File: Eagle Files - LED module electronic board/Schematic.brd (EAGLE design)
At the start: 30.5 x 30.5 mm, 14 parts, among them IC1 AMS1117-1.5, IC2 LM358N, J1 2.54 CONN, J2 2.54 CONN, Q1 P16NF06L

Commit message: Update
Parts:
- removed J1, J2: 2.54 CONN, SparkFun-Connectors:1X02
- removed Q1: P16NF06L, adafruit:TO220V
- removed R3: 10k, LED-microscope-library:HDRV3W64P254_1X3_1016X508X838B
- added Q2: P16NF06L, transistor-power:TO220BV
- added U$1: (no value), untitled:POT-SWITCH-PTH
- added U$3, U$4: (no value), untitled:1X02_NO_SILK
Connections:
- new net N$10: IC2.5, U$1.2
- net GND: now also U$1.3, U$3.2; no longer J1.1, R3.1
- net N$1: now also U$1.5, U$3.1; no longer IC2.5, R3.3
- net N$4: now also U$1.1; no longer R3.2
- net N$5: now also Q2.D, U$4.1; no longer J2.2, Q1.2
- net N$7: now also Q2.G; no longer Q1.1
- net N$9: now also Q2.S; no longer Q1.3
- net VCC: now also U$1.4, U$4.2; no longer J1.2, J2.1
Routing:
- net N$10: track 0.00 -> 20.1 mm, vias 0 -> 1
- net N$5: track 20.6 -> 26.9 mm
- net N$4: track 11.3 -> 17.1 mm
- net N$1: track 16.2 -> 17.1 mm
- net N$9: track 19.0 -> 19.6 mm

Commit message: Major changes!
Major changes! Do not use older version, pins swapped in V-regulator.
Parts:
- removed IC1: AMS1117-1.5, linear:SOT223
- added U$2: VREG-AMS1117-1.5, untitled:SOT230P700X180-4
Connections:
- net GND: now also U$2.1; no longer IC1.4
- net N$3: now also U$2.2, U$2.4; no longer IC1.3
- net VCC: now also U$2.3; no longer IC1.1
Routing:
- net N$3: track 15.9 -> 18.6 mm
- net VCC: track 40.9 -> 39.7 mm
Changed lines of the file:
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@@
 </layers>
 <board>
-<fusionsync huburn="a.cGVyc29uYWw6dWUyYjI2N2I0" projecturn="a.cGVyc29uYWw6dWUyYjI2N2I0IzIwMTcwOTAxOTA2NzgyODE" f3durn="urn:adsk.wipprod:dm.lineage:6GncY3L6S8qHhpXXGHIO-A" pcbguid="c076c7f6-f98b-4770-9c04-7120ef74dbe8" lastpulledtime="" lastsyncedchangeguid="168a07d3-ac94-f938-486a-87856d6dfaa1"/>
+<fusionsync huburn="a.cGVyc29uYWw6dWUyYjI2N2I0" projecturn="a.cGVyc29uYWw6dWUyYjI2N2I0IzIwMTcwOTAxOTA2NzgyODE" f3durn="urn:adsk.wipprod:dm.lineage:6GncY3L6S8qHhpXXGHIO-A" pcbguid="c076c7f6-f98b-4770-9c04-7120ef74dbe8" lastpulledtime="" lastsyncedchangeguid="b84cecf9-df35-d3de-ebe7-257acc63ca98"/>
 <plain>
 <wire x1="1.5875" y1="68.2625" x2="32.0475" y2="68.2625" width="0" layer="20"/>
@@
 <attribute name="VALUE" x="25.781" y="88.9635" size="1.27" layer="27" ratio="10" rot="R270"/>
 </element>
-<element name="IC1" library="linear" library_urn="urn:adsk.eagle:library:262" package="SOT223" package3d_urn="urn:adsk.eagle:package:28541/2" value="AMS1117-1.5" x="8.255" y="83.82" smashed="yes" rot="MR0">
-<attribute name="NAME" x="4.445" y="81.9658" size="1.27" layer="26" rot="MR0"/>
-<attribute name="VALUE" x="10.795" y="82.4992" size="1.27" layer="28" rot="MR0"/>
-</element>
 <element name="IC2" library="linear" library_urn="urn:adsk.eagle:library:262" package="DIL08" package3d_urn="urn:adsk.eagle:package:16409/2" value="LM358N" x="20.955" y="83.82" smashed="yes" rot="R270">
 <attribute name="NAME" x="18.034" y="89.154" size="1.27" layer="25" ratio="10"/>
@@
 <attribute name="VALUE" x="23.495" y="83.185" size="1.27" layer="27" ratio="10" rot="R270"/>
 </element>
+<element name="U$2" library="untitled" library_urn="urn:adsk.eagle:library:8804918" package="SOT230P700X180-4" package3d_urn="urn:adsk.eagle:package:9947855/1" value="VREG-AMS1117-1.5" x="8.255" y="83.5025" smashed="yes" rot="MR270">
+<attribute name="NAME" x="4.1214" y="83.5025" size="1.27" layer="26" rot="MR270" align="bottom-center"/>
+<attribute name="VALUE" x="12.24" y="83.5025" size="1.27" layer="28" rot="MR270" align="top-center"/>
+</element>
 </elements>
 <signals>
 <signal name="GND">
-<contactref element="IC1" pad="4"/>
 <contactref element="IC2" pad="4"/>
 <contactref element="R2" pad="1"/>
@@
 <contactref element="U$3" pad="2"/>
 <contactref element="U$1" pad="3"/>
-<wire x1="8.255" y1="86.919" x2="8.255" y2="94.615" width="0" layer="19" extent="16-16"/>
-<wire x1="4.705" y1="86.36" x2="8.255" y2="86.919" width="0" layer="19" extent="1-16"/>
-<wire x1="14.605" y1="88.417" x2="8.255" y2="86.919" width="0" layer="19" extent="16-16"/>
-<wire x1="6.655" y1="78.74" x2="4.705" y2="86.36" width="0" layer="19" extent="1-1"/>
+<contactref element="U$2" pad="1"/>
+<wire x1="8.255" y1="94.615" x2="15.955" y2="97.155" width="0" layer="19" extent="1-1"/>
+<wire x1="14.605" y1="88.417" x2="15.955" y2="97.155" width="0" layer="19" extent="16-16"/>
 <wire x1="17.145" y1="80.01" x2="14.605" y2="88.417" width="0" layer="19" extent="16-16"/>
 <wire x1="23.755" y1="75.565" x2="17.145" y2="80.01" width="0" layer="19" extent="1-1"/>
-<wire x1="15.955" y1="97.155" x2="6.655" y2="78.74" width="0" layer="19" extent="1-1"/>
+<wire x1="4.705" y1="86.36" x2="8.255" y2="94.615" width="0" layer="19" extent="1-1"/>
+<wire x1="6.655" y1="78.74" x2="4.705" y2="86.36" width="0" layer="19" extent="1-1"/>
+<wire x1="5.955" y1="86.5251" x2="6.655" y2="78.74" width="0" layer="19" extent="1-1"/>
 </signal>
 <signal name="N$3">
-<contactref element="IC1" pad="3"/>
 <contactref element="R1" pad="1"/>
 <contactref element="C2" pad="+"/>
-<wire x1="5.7023" y1="80.8101" x2="5.9436" y2="80.7212" width="0.3556" layer="16"/>
-<wire x1="9.855" y1="78.74" x2="9.855" y2="77.775" width="0.3556" layer="1"/>
-<wire x1="5.9436" y1="80.7212" x2="6.0325" y2="80.6323" width="0.3556" layer="16"/>
+<wire x1="9.855" y1="77.775" x2="9.855" y2="78.74" width="0.3556" layer="1"/>
 <wire x1="14.453" y1="79.223" x2="14.605" y2="79.223" width="0.3556" layer="16"/>
 <wire x1="14.605" y1="79.223" x2="12.5345" y2="77.1525" width="0.3556" layer="16"/>
-<wire x1="12.5345" y1="77.1525" x2="8.255" y2="77.1525" width="0.3556" layer="16"/>
-<wire x1="9.855" y1="77.775" x2="9.2325" y2="77.1525" width="0.3556" layer="1"/>
-<wire x1="9.2325" y1="77.1525" x2="8.255" y2="77.1525" width="0.3556" layer="1"/>
-<via x="8.255" y="77.1525" extent="1-16" drill="0.3556"/>
-<wire x1="8.255" y1="77.1525" x2="6.6675" y2="77.1525" width="0.3556" layer="16"/>
-<wire x1="6.6675" y1="77.1525" x2="6.0325" y2="77.7875" width="0.3556" layer="16"/>
-<wire x1="6.0325" y1="77.7875" x2="6.0325" y2="80.6323" width="0.3556" layer="16"/>
+<via x="10.7127" y="77.1525" extent="1-16" drill="0.3556"/>
+<wire x1="10.7127" y1="77.1525" x2="10.16" y2="77.1525" width="0.356" layer="1"/>
+<wire x1="10.16" y1="77.1525" x2="9.855" y2="77.4575" width="0.356" layer="1"/>
+<wire x1="9.855" y1="77.4575" x2="9.855" y2="77.775" width="0.356" layer="1"/>
+<wire x1="12.5345" y1="77.1525" x2="10.7127" y2="77.1525" width="0.356" layer="16"/>
+<wire x1="8.89" y1="77.1525" x2="8.255" y2="77.7875" width="0.356" layer="16"/>
+<wire x1="8.89" y1="77.1525" x2="10.7127" y2="77.1525" width="0.356" layer="16"/>
+<contactref element="U$2" pad="2"/>
+<contactref element="U$2" pad="4"/>
+<wire x1="8.255" y1="77.7875" x2="8.255" y2="80.4799" width="0.356" layer="16"/>
+<wire x1="8.255" y1="80.4799" x2="8.255" y2="86.5251" width="1.067" layer="16"/>
 </signal>
 <signal name="VCC">
-<contactref element="IC1" pad="1"/>
 <contactref element="C1" pad="+"/>
 <contactref element="IC2" pad="8"/>
-<wire x1="10.45754375" y1="80.645" x2="10.5664" y2="80.7212" width="0.3556" layer="16"/>
-<wire x1="10.16" y1="81.1276" x2="10.5664" y2="80.7212" width="0.3556" layer="16"/>
 <wire x1="24.765" y1="87.63" x2="23.495" y2="86.36" width="0.3556" layer="1"/>
 <wire x1="23.495" y1="86.36" x2="11.805" y2="86.36" width="0.3556" layer="1"/>
-<wire x1="10.5664" y1="80.7212" x2="10.6426" y2="80.645" width="1.067" layer="16"/>
 <wire x1="11.805" y1="86.36" x2="11.805" y2="83.82" width="1.067" layer="1"/>
-<wire x1="10.5664" y1="80.7212" x2="10.5664" y2="82.5814" width="1.067" layer="16"/>
-<wire x1="10.5664" y1="82.5814" x2="11.805" y2="83.82" width="1.067" layer="16"/>
 <via x="11.805" y="83.82" extent="1-16" drill="1.067"/>
 <wire x1="11.7475" y1="86.4175" x2="11.805" y2="86.36" width="1.067" layer="1"/>
@@
 <wire x1="11.805" y1="73.4" x2="10.795" y2="72.39" width="1.067" layer="1"/>
 <wire x1="11.805" y1="83.82" x2="11.805" y2="73.4" width="1.067" layer="1"/>
+<contactref element="U$2" pad="3"/>
+<wire x1="10.555" y1="85.07" x2="10.555" y2="86.5251" width="1.067" layer="16"/>
+<wire x1="11.805" y1="83.82" x2="10.555" y2="85.07" width="1.067" layer="16"/>
 </signal>
 <signal name="N$2">

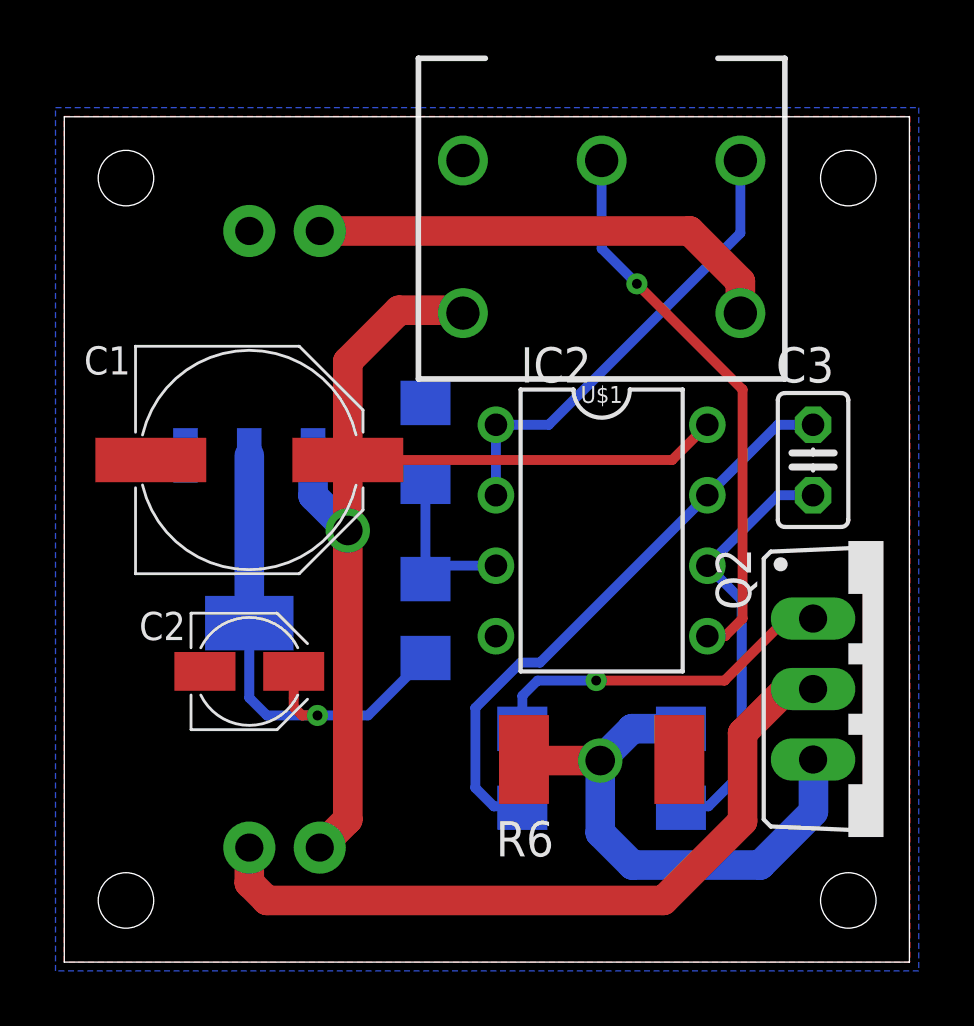
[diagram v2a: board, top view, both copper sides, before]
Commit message: Minor changes in footprints
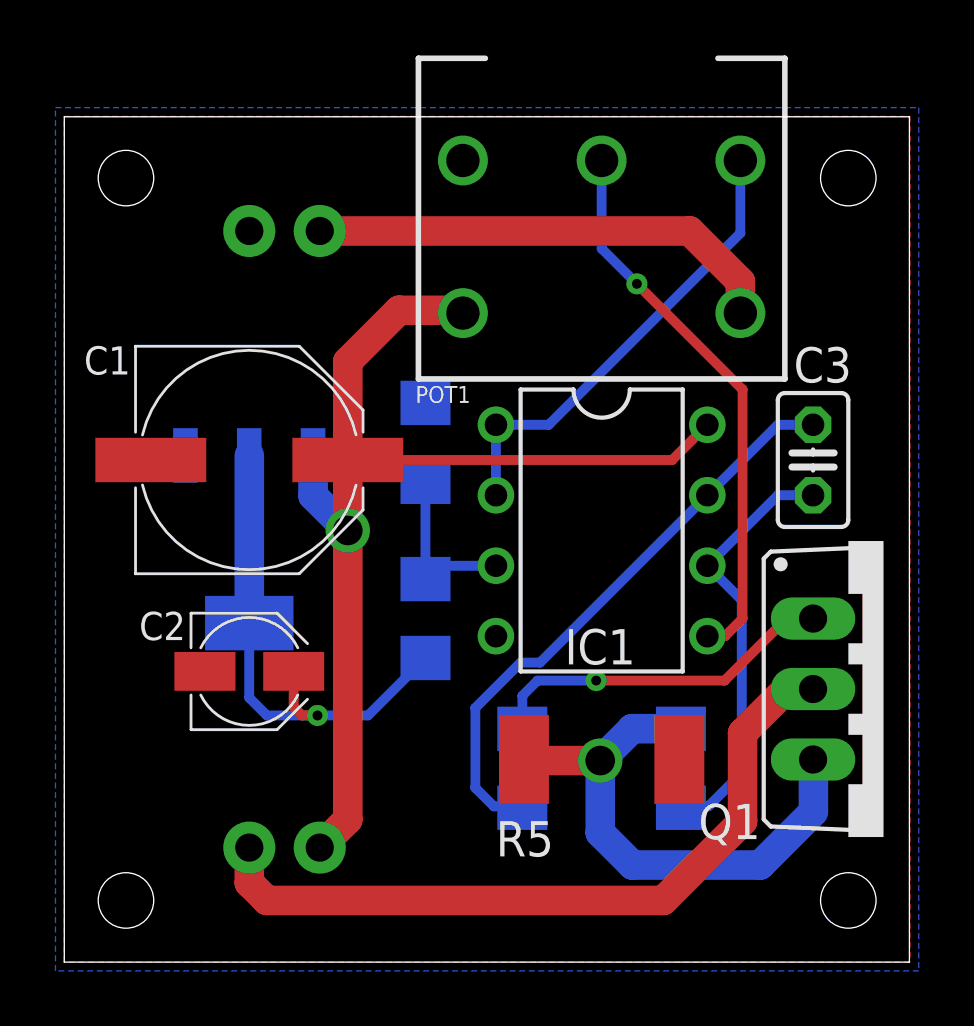
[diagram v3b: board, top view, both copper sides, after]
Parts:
- removed R6: 0.05, rcl:R2512
- added R3: 220, rcl:R1206
- R4: value 220 -> 10k
- R5: value 10k -> 0.05; device rcl:R1206 -> rcl:R2512
- moved R4 5.71 mm to (23.8, 75.2)
- moved R5 2.88 mm to (21.0, 75.6), flipped to the top, turned to 0 degrees
- renumbered IC2 to IC1, Q2 to Q1, U$1 to POT1, U$2 to U1, U$3 to J1, U$4 to J2
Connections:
- net GND: now also R5.2; no longer R6.2
- net N$6: now also R3.2; no longer R4.2
- net N$7: now also R3.1; no longer R4.1
- net N$8: now also R4.2; no longer R5.2
- net N$9: now also R4.1; no longer R6.1
